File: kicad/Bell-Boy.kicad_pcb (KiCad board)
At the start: 2 copper layers, 64 x 30 mm, 35 parts, among them J1 Conn_01x01_Male, J2 Conn_01x06, J3 Conn_01x04, J4 Conn_02x16_Odd_Even, SW1 SW_DIP_x01, U1 ATmega328P-AU, U2 MAX40200, U3 MCP73831-2-OT, U4 MAX40200, U5 ICM-20689

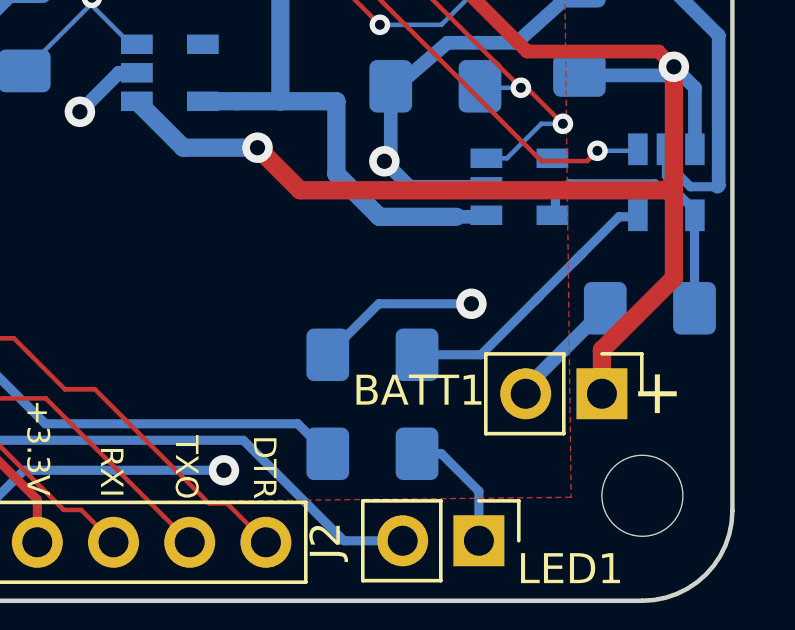
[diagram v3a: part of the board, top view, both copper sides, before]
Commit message: PCB updates, scales now easier to read
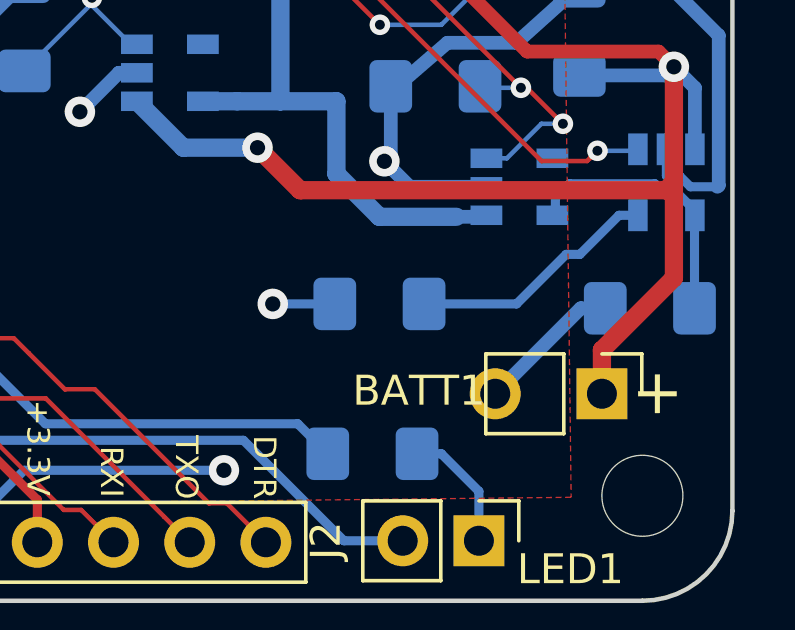
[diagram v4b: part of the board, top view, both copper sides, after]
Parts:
- moved R3 1.71 mm to (102.2, 70.1)
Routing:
- net GND: track 171.6 -> 169.1 mm
- net Net-(R3-Pad1): track 9.85 -> 8.35 mm
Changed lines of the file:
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@@
     (thickness 1.6)
     (drawings 25)
-    (tracks 612)
+    (tracks 609)
     (zones 0)
     (modules 35)
@@
   )
   (setup
-    (last_trace_width 0.6096)
+    (last_trace_width 0.4572)
     (user_trace_width 0.1524)
     (user_trace_width 0.3048)
@@
     (mod_text_size 1 1)
     (mod_text_width 0.15)
-    (pad_size 2.7 2.7)
-    (pad_drill 2.7)
+    (pad_size 1.7 1.7)
+    (pad_drill 1)
     (pad_to_mask_clearance 0.0762)
     (solder_mask_min_width 0.254)
@@
   )
   (module Resistor_SMD:R_1206_3216Metric_Pad1.42x1.75mm_HandSolder (layer B.Cu)
-    (at 102 71.8 180)
+    (at 102.235 70.104 180)
     (descr "Resistor SMD 1206 (3216 Metric), square (rectangular) end terminal, IPC_7351 nominal with elongated pad for handsoldering. (Body size source: http://www.tortai-tech.com/upload/download/2011102023233369053.pdf), generated with kicad-footprint-generator")
     (tags "resistor handsolder")
     (attr smd)
-    (fp_text reference R3 (at 3.3 0.04 180) (layer B.SilkS)
+    (fp_text reference R3 (at 0.127 1.524 180) (layer B.SilkS)
       (effects (font (size 1 1) (thickness 0.15)) (justify mirror))
     )
@@
     (pad 1 thru_hole rect (at 0 0 270) (size 1.7 1.7) (drill 1) (layers *.Cu *.Mask)
       (net 4 +BATT))
-    (pad 2 thru_hole oval (at 0 2.54 270) (size 1.7 1.7) (drill 1) (layers *.Cu *.Mask)
+    (pad 2 thru_hole oval (at 0 3.556 270) (size 1.7 1.7) (drill 1) (layers *.Cu *.Mask)
       (net 3 GND))
     (model ${KISYS3DMOD}/Connector_PinHeader_2.54mm.3dshapes/PinHeader_1x02_P2.54mm_Vertical.wrl
@@
     (descr "Through hole straight pin header, 1x01, 2.54mm pitch, single row")
     (tags "Through hole pin header THT 1x01 2.54mm single row")
-    (fp_text reference J1 (at 0 2.33 90) (layer B.SilkS)
+    (fp_text reference J1 (at 0.011 -1.905 90) (layer B.SilkS)
       (effects (font (size 1 1) (thickness 0.15)) (justify mirror))
     )
@@
   (segment (start 51.5 60.421502) (end 51.5 61.5) (width 0.6096) (layer F.Cu) (net 3))
   (segment (start 58.221502 53.7) (end 51.5 60.421502) (width 0.6096) (layer F.Cu) (net 3))
-  (via (at 105.3 70.1) (size 1.016) (drill 0.508) (layers F.Cu B.Cu) (net 3))
-  (segment (start 100.5125 71.8) (end 102.2125 70.1) (width 0.3048) (layer B.Cu) (net 3) (status 10))
-  (segment (start 102.2125 70.1) (end 105.3 70.1) (width 0.3048) (layer B.Cu) (net 3))
   (segment (start 113.54399 66.15601) (end 113.5 66.2) (width 0.4572) (layer B.Cu) (net 3))
   (segment (start 113.54399 61.15399) (end 113.54399 66.15601) (width 0.4572) (layer B.Cu) (net 3))
   (segment (start 111.9025 59.5125) (end 113.54399 61.15399) (width 0.4572) (layer B.Cu) (net 3))
-  (segment (start 107.11 72.9025) (end 109.7625 70.25) (width 0.4572) (layer B.Cu) (net 3) (status 30))
-  (segment (start 107.11 73.1) (end 107.11 72.9025) (width 0.4572) (layer B.Cu) (net 3) (status 30))
   (segment (start 77.4 59.0625) (end 77.45 59.1125) (width 0.6096) (layer B.Cu) (net 3) (status 30))
   (segment (start 70.05 59.0625) (end 77.4 59.0625) (width 0.6096) (layer B.Cu) (net 3) (status 30))
@@
   (segment (start 90.4 59.3625) (end 88.519 61.2435) (width 0.4572) (layer B.Cu) (net 3))
   (segment (start 88.519 61.2435) (end 88.519 64.135) (width 0.4572) (layer B.Cu) (net 3))
+  (via (at 98.679 70.104) (size 1.016) (drill 0.508) (layers F.Cu B.Cu) (net 3))
+  (segment (start 100.7475 70.104) (end 98.679 70.104) (width 0.3048) (layer B.Cu) (net 3))
+  (segment (start 108.944 70.25) (end 109.7625 70.25) (width 0.4572) (layer B.Cu) (net 3))
+  (segment (start 106.094 73.1) (end 108.944 70.25) (width 0.4572) (layer B.Cu) (net 3))
   (segment (start 111.7625 62.4875) (end 112.05 62.2) (width 0.4572) (layer B.Cu) (net 4))
   (segment (start 108.9 62.4875) (end 111.7625 62.4875) (width 0.4572) (layer B.Cu) (net 4) (status 10))
@@
   (segment (start 61.395822 56.85) (end 64.3 56.85) (width 0.1524) (layer F.Cu) (net 11))
   (segment (start 64.3 56.85) (end 64.7 56.85) (width 0.1524) (layer F.Cu) (net 11))
-  (segment (start 110.2202 67.2) (end 110.85 67.2) (width 0.3048) (layer B.Cu) (net 12) (status 20))
-  (segment (start 108.7202 68.7) (end 109 68.4202) (width 0.3048) (layer B.Cu) (net 12))
-  (segment (start 109 68.4202) (end 110.2202 67.2) (width 0.3048) (layer B.Cu) (net 12))
-  (segment (start 105.6202 71.8) (end 107.55 69.8702) (width 0.3048) (layer B.Cu) (net 12))
-  (segment (start 103.4875 71.8) (end 105.6202 71.8) (width 0.3048) (layer B.Cu) (net 12) (status 10))
-  (segment (start 107.4202 70) (end 107.55 69.8702) (width 0.3048) (layer B.Cu) (net 12))
-  (segment (start 107.55 69.8702) (end 109 68.4202) (width 0.3048) (layer B.Cu) (net 12))
+  (segment (start 110.2202 67.15) (end 108.9172 68.453) (width 0.3048) (layer B.Cu) (net 12))
+  (segment (start 110.85 67.15) (end 110.2202 67.15) (width 0.3048) (layer B.Cu) (net 12))
+  (segment (start 108.9172 68.453) (end 108.458 68.453) (width 0.3048) (layer B.Cu) (net 12))
+  (segment (start 106.807 70.104) (end 103.7225 70.104) (width 0.3048) (layer B.Cu) (net 12))
+  (segment (start 108.458 68.453) (end 106.807 70.104) (width 0.3048) (layer B.Cu) (net 12))
   (segment (start 112.7875 67.2375) (end 112.75 67.2) (width 0.3048) (layer B.Cu) (net 13) (status 30))
   (segment (start 112.75 66.995) (end 112.75 67.2) (width 0.3048) (layer B.Cu) (net 13) (status 30))

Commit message: Minor updates
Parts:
- moved R1 3.12 mm to (100.1, 72.6)
- moved BATT1 1.58 mm to (108.1, 73.3)
- moved R3 0.38 mm to (102.2, 69.7)
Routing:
- net Net-(LED1-Pad1): track 4.28 -> 8.40 mm
- net Net-(R1-Pad2): track 50.8 -> 47.9 mm
- net GND: track 169.1 -> 171.7 mm
- net +BATT: track 54.1 -> 55.8 mm
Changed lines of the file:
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@@
     (thickness 1.6)
     (drawings 25)
-    (tracks 609)
+    (tracks 615)
     (zones 0)
     (modules 35)
@@
   )
   (setup
-    (last_trace_width 0.4572)
+    (last_trace_width 0.6096)
     (user_trace_width 0.1524)
     (user_trace_width 0.3048)
@@
   )
   (module Resistor_SMD:R_1206_3216Metric_Pad1.42x1.75mm_HandSolder (layer B.Cu)
-    (at 102 75.1 180)
+    (at 100.076 72.644 180)
     (descr "Resistor SMD 1206 (3216 Metric), square (rectangular) end terminal, IPC_7351 nominal with elongated pad for handsoldering. (Body size source: http://www.tortai-tech.com/upload/download/2011102023233369053.pdf), generated with kicad-footprint-generator")
     (tags "resistor handsolder")
     (attr smd)
-    (fp_text reference R1 (at -3.25 0.05 180) (layer B.SilkS)
+    (fp_text reference R1 (at 3.556 -0.381 180) (layer B.SilkS)
       (effects (font (size 1 1) (thickness 0.15)) (justify mirror))
     )
@@
   )
   (module Resistor_SMD:R_1206_3216Metric_Pad1.42x1.75mm_HandSolder (layer B.Cu)
-    (at 102.235 70.104 180)
+    (at 102.235 69.723 180)
     (descr "Resistor SMD 1206 (3216 Metric), square (rectangular) end terminal, IPC_7351 nominal with elongated pad for handsoldering. (Body size source: http://www.tortai-tech.com/upload/download/2011102023233369053.pdf), generated with kicad-footprint-generator")
     (tags "resistor handsolder")
@@
   )
   (module Connector_PinHeader_2.54mm:PinHeader_1x02_P2.54mm_Vertical (layer F.Cu)
-    (at 109.65 73.1 270)
+    (at 108.077 73.279 270)
     (descr "Through hole straight pin header, 1x02, 2.54mm pitch, single row")
     (tags "Through hole pin header THT 1x02 2.54mm single row")
-    (fp_text reference BATT1 (at -0.1 6.1) (layer F.SilkS)
+    (fp_text reference BATT1 (at 2.159 1.651) (layer F.SilkS)
       (effects (font (size 1 1) (thickness 0.15)))
     )
@@
     (effects (font (size 0.75 0.75) (thickness 0.1875)) (justify mirror))
   )
-  (gr_text + (at 111.5 73.05) (layer F.SilkS)
+  (gr_text + (at 110.109 72.517) (layer F.SilkS)
     (effects (font (size 1.5 1.5) (thickness 0.3)))
   )
@@
   (segment (start 90.4 59.3625) (end 88.519 61.2435) (width 0.4572) (layer B.Cu) (net 3))
   (segment (start 88.519 61.2435) (end 88.519 64.135) (width 0.4572) (layer B.Cu) (net 3))
-  (via (at 98.679 70.104) (size 1.016) (drill 0.508) (layers F.Cu B.Cu) (net 3))
-  (segment (start 100.7475 70.104) (end 98.679 70.104) (width 0.3048) (layer B.Cu) (net 3))
-  (segment (start 108.944 70.25) (end 109.7625 70.25) (width 0.4572) (layer B.Cu) (net 3))
-  (segment (start 106.094 73.1) (end 108.944 70.25) (width 0.4572) (layer B.Cu) (net 3))
+  (via (at 98.425 69.723) (size 0.6858) (drill 0.3302) (layers F.Cu B.Cu) (net 3))
+  (segment (start 100.7475 69.723) (end 98.425 69.723) (width 0.3048) (layer B.Cu) (net 3))
+  (segment (start 108.95 70.25) (end 109.7625 70.25) (width 0.6096) (layer B.Cu) (net 3))
+  (segment (start 106.347919 70.25) (end 108.95 70.25) (width 0.6096) (layer B.Cu) (net 3))
+  (segment (start 104.521 72.076919) (end 106.347919 70.25) (width 0.6096) (layer B.Cu) (net 3))
+  (segment (start 104.521 73.279) (end 104.521 72.076919) (width 0.6096) (layer B.Cu) (net 3))
   (segment (start 111.7625 62.4875) (end 112.05 62.2) (width 0.4572) (layer B.Cu) (net 4))
   (segment (start 108.9 62.4875) (end 111.7625 62.4875) (width 0.4572) (layer B.Cu) (net 4) (status 10))
@@
   (segment (start 112.75 65) (end 112.75 62.9) (width 0.4572) (layer B.Cu) (net 4) (status 10))
   (via (at 112.05 62.2) (size 1.016) (drill 0.508) (layers F.Cu B.Cu) (net 4))
-  (segment (start 109.65 71.6404) (end 112.05 69.2404) (width 0.6096) (layer F.Cu) (net 4))
-  (segment (start 109.65 73.1) (end 109.65 71.6404) (width 0.6096) (layer F.Cu) (net 4) (status 10))
   (segment (start 112.05 66.05) (end 111.860999 66.239001) (width 0.4572) (layer F.Cu) (net 4))
   (segment (start 112.05 66.05) (end 112.05 62.2) (width 0.6096) (layer F.Cu) (net 4))
@@
   (segment (start 99.589201 66.315201) (end 111.784799 66.315201) (width 0.6096) (layer F.Cu) (net 4))
   (segment (start 98.171 64.897) (end 99.589201 66.315201) (width 0.6096) (layer F.Cu) (net 4))
+  (segment (start 112.05 70.7656) (end 112.05 69.2404) (width 0.6096) (layer F.Cu) (net 4))
+  (segment (start 109.5366 73.279) (end 112.05 70.7656) (width 0.6096) (layer F.Cu) (net 4))
+  (segment (start 108.077 73.279) (end 109.5366 73.279) (width 0.6096) (layer F.Cu) (net 4))
   (segment (start 71.2875 67.65) (end 71.3375 67.7) (width 0.1524) (layer B.Cu) (net 5) (status 30))
   (via (at 64.5 76.25) (size 0.6858) (drill 0.3302) (layers F.Cu B.Cu) (net 5))
@@
   (segment (start 57.3 64.9) (end 57.3 66.7) (width 0.3048) (layer B.Cu) (net 9) (status 10))
   (segment (start 57.3 66.7) (end 57 67) (width 0.3048) (layer B.Cu) (net 9))
-  (segment (start 100.5125 75.1) (end 99.5125 74.1) (width 0.3048) (layer B.Cu) (net 9) (status 10))
   (segment (start 57 67) (end 57.45 67.45) (width 0.3048) (layer F.Cu) (net 9))
   (via (at 89.05 72.05) (size 0.6858) (drill 0.3302) (layers F.Cu B.Cu) (net 9))
-  (segment (start 99.5125 74.1) (end 91.1 74.1) (width 0.3048) (layer B.Cu) (net 9))
-  (segment (start 91.1 74.1) (end 89.05 72.05) (width 0.3048) (layer B.Cu) (net 9))
   (segment (start 78.810897 68.997701) (end 71.047701 68.997701) (width 0.3048) (layer F.Cu) (net 9))
   (segment (start 84.442181 68.73101) (end 79.077588 68.73101) (width 0.3048) (layer F.Cu) (net 9))
@@
   (segment (start 87.207101 71.49593) (end 86.95 71.238829) (width 0.3048) (layer F.Cu) (net 9))
   (segment (start 86.95 71.238829) (end 84.442181 68.73101) (width 0.3048) (layer F.Cu) (net 9))
+  (segment (start 97.9945 72.05) (end 98.5885 72.644) (width 0.3048) (layer B.Cu) (net 9))
+  (segment (start 89.05 72.05) (end 97.9945 72.05) (width 0.3048) (layer B.Cu) (net 9))
   (via (at 62.243799 65.006201) (size 0.6858) (drill 0.3302) (layers F.Cu B.Cu) (net 10))
   (segment (start 62.243799 68.408601) (end 62.243799 65.006201) (width 0.1524) (layer B.Cu) (net 10))
@@
   (segment (start 110.2202 67.15) (end 108.9172 68.453) (width 0.3048) (layer B.Cu) (net 12))
   (segment (start 110.85 67.15) (end 110.2202 67.15) (width 0.3048) (layer B.Cu) (net 12))
-  (segment (start 108.9172 68.453) (end 108.458 68.453) (width 0.3048) (layer B.Cu) (net 12))
-  (segment (start 106.807 70.104) (end 103.7225 70.104) (width 0.3048) (layer B.Cu) (net 12))
-  (segment (start 108.458 68.453) (end 106.807 70.104) (width 0.3048) (layer B.Cu) (net 12))
+  (segment (start 105.805 68.453) (end 108.712 68.453) (width 0.3048) (layer B.Cu) (net 12))
+  (segment (start 104.535 69.723) (end 105.805 68.453) (width 0.3048) (layer B.Cu) (net 12))
+  (segment (start 103.7225 69.723) (end 104.535 69.723) (width 0.3048) (layer B.Cu) (net 12))
+  (segment (start 108.9172 68.453) (end 108.712 68.453) (width 0.3048) (layer B.Cu) (net 12))
+  (segment (start 108.712 68.453) (end 108.458 68.453) (width 0.3048) (layer B.Cu) (net 12))
   (segment (start 112.7875 67.2375) (end 112.75 67.2) (width 0.3048) (layer B.Cu) (net 13) (status 30))
   (segment (start 112.75 66.995) (end 112.75 67.2) (width 0.3048) (layer B.Cu) (net 13) (status 30))
@@
   (segment (start 60.7 70.65) (end 64.35 70.65) (width 0.3048) (layer F.Cu) (net 15))
   (segment (start 105.5875 77.9625) (end 105.55 78) (width 0.3048) (layer B.Cu) (net 16) (status 30))
-  (segment (start 105.55 76.35) (end 105.55 78) (width 0.3048) (layer B.Cu) (net 16) (status 20))
-  (segment (start 104.3 75.1) (end 105.55 76.35) (width 0.3048) (layer B.Cu) (net 16))
-  (segment (start 103.4875 75.1) (end 104.3 75.1) (width 0.3048) (layer B.Cu) (net 16) (status 10))
+  (segment (start 105.55 76.8452) (end 104.6508 75.946) (width 0.3048) (layer B.Cu) (net 16))
+  (segment (start 105.55 78) (end 105.55 76.8452) (width 0.3048) (layer B.Cu) (net 16))
+  (segment (start 104.6508 75.946) (end 102.362 75.946) (width 0.3048) (layer B.Cu) (net 16))
+  (segment (start 101.5635 75.1475) (end 101.5635 72.644) (width 0.3048) (layer B.Cu) (net 16))
+  (segment (start 102.362 75.946) (end 101.5635 75.1475) (width 0.3048) (layer B.Cu) (net 16))
   (segment (start 58.9 64.9) (end 58.9 66.1) (width 0.1524) (layer B.Cu) (net 17) (status 10))
   (segment (start 58.9 66.1) (end 58.95 66.15) (width 0.1524) (layer B.Cu) (net 17))
